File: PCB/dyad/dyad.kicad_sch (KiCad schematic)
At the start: 7 parts, among them SW1 SW_SPST, SW2 SW_SPST, SW3 SW_SPST, SW4 SW_SPST, SW5 SW_SPST, SW6 SW_SPST

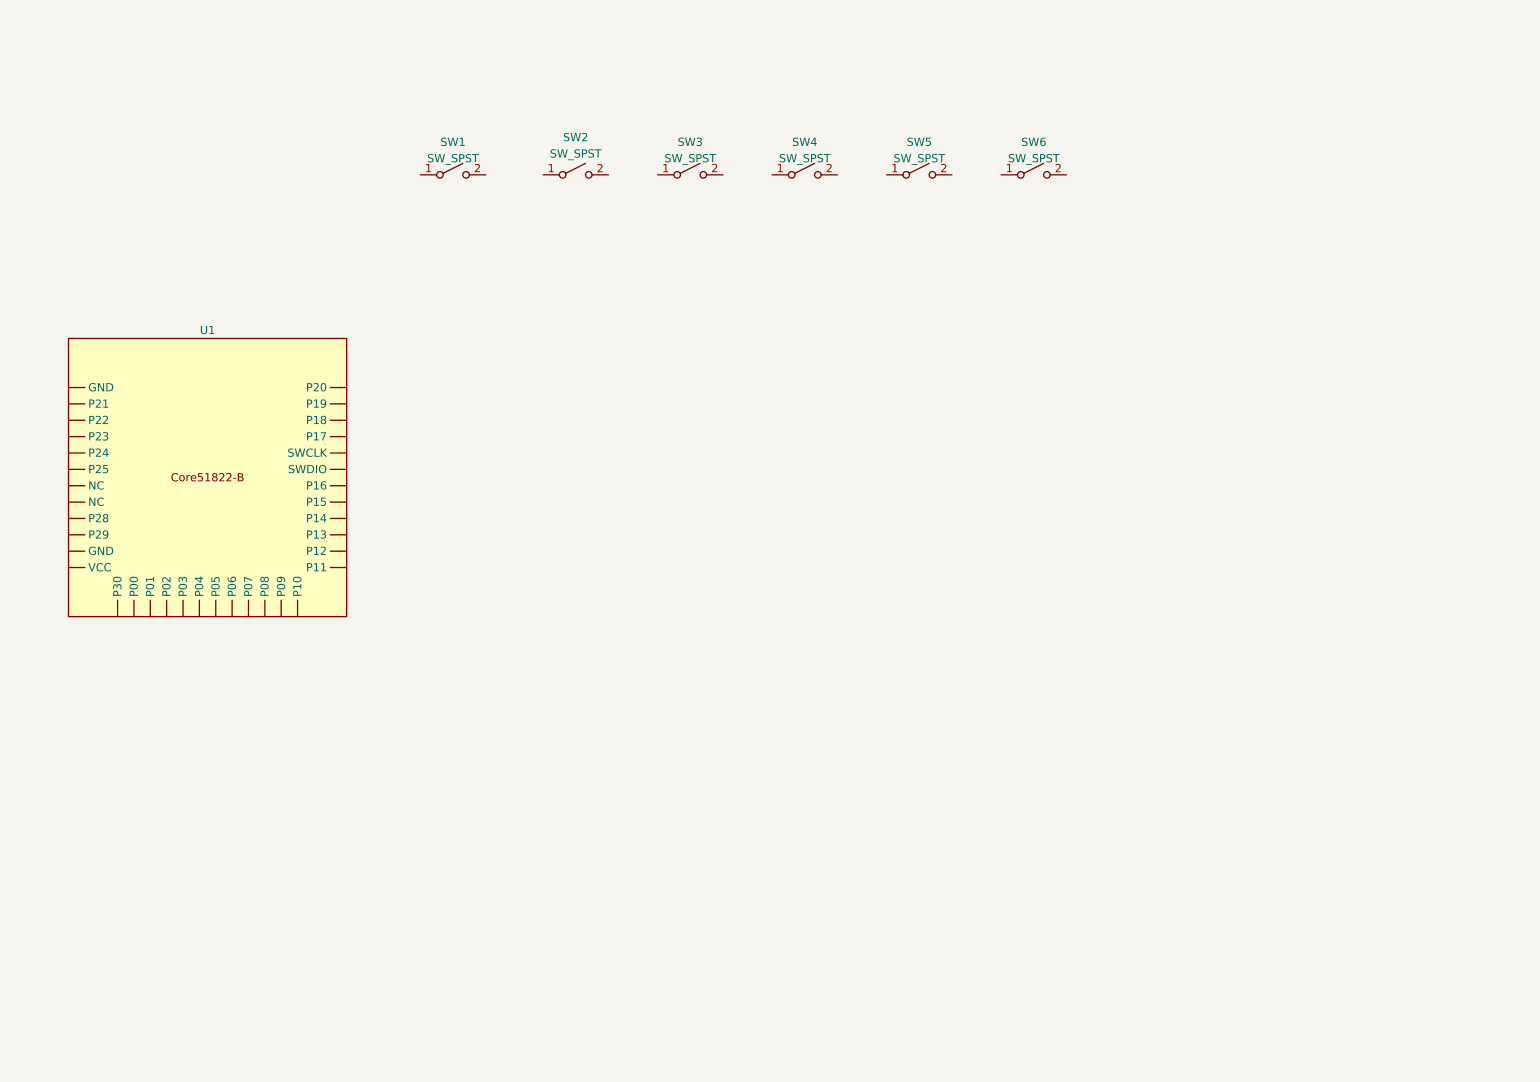
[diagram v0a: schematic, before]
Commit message: add diodes
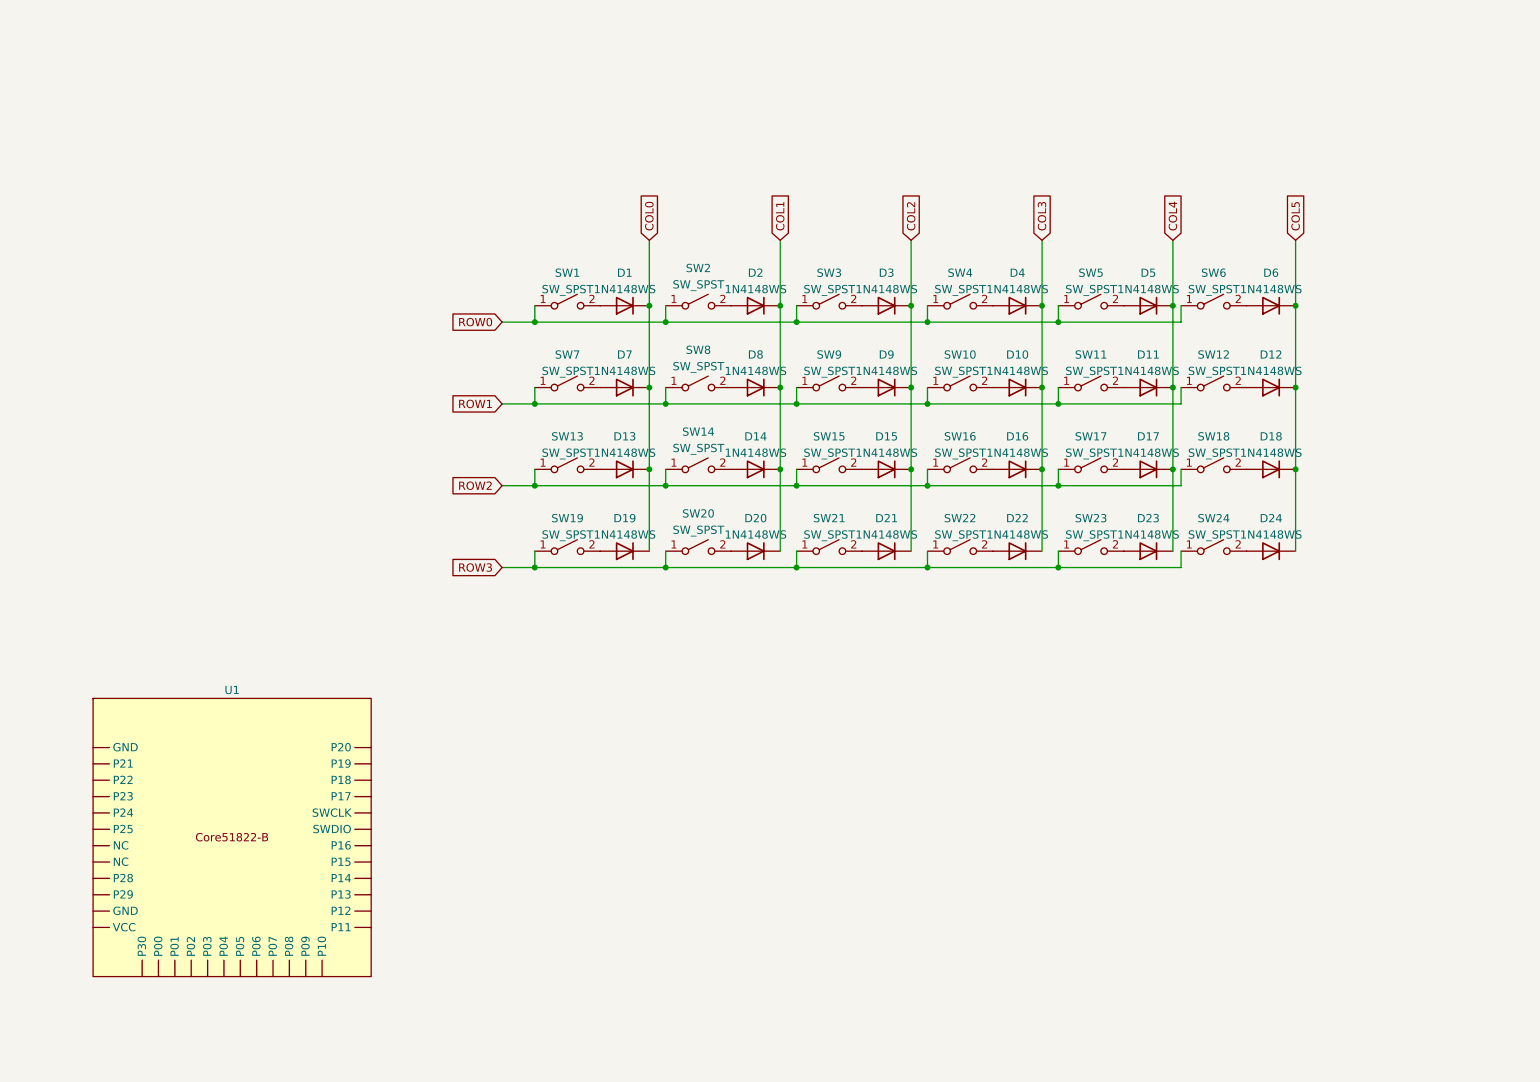
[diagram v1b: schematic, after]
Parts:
- added D1, D10, D11, D12, D13, D14, D15, D16, D17, D18, D19, D2, D20, D21, D22, D23, D24, D3, D4, D5, D6, D7, D8, D9: 1N4148WS, Diode_SMD:D_SOD-323, symbol Diode:1N4148WS
- added SW10, SW11, SW12, SW13, SW14, SW15, SW16, SW17, SW18, SW19, SW20, SW21, SW22, SW23, SW24, SW7, SW8, SW9: SW_SPST, keyswitches.pretty-master:Kailh_socket_MX, symbol Switch:SW_SPST
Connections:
- net ROW0: now reaches SW6.1 (A)
- net ROW0: now also SW1.1 (A), SW2.1 (A), SW3.1 (A), SW4.1 (A), SW5.1 (A)
- net at SW6.2 (B): now also D6.2 (A)
- net at SW5.2 (B): now also D5.2 (A)
- net at SW1.2 (B): now also D1.2 (A)
- net at SW3.2 (B): now also D3.2 (A)
- net at SW2.2 (B): now also D2.2 (A)
- net at SW4.2 (B): now also D4.2 (A)
- new net: D22.2 (A), SW22.2 (B)
- new net: D21.2 (A), SW21.2 (B)
- new net: D15.2 (A), SW15.2 (B)
- new net: D16.2 (A), SW16.2 (B)
- new net: D10.2 (A), SW10.2 (B)
- new net: D9.2 (A), SW9.2 (B)
- new net: D11.2 (A), SW11.2 (B)
- new net: D23.2 (A), SW23.2 (B)
- new net: D18.2 (A), SW18.2 (B)
- new net: D24.2 (A), SW24.2 (B)
- new net: D8.2 (A), SW8.2 (B)
- new net: D20.2 (A), SW20.2 (B)
- new net: D12.2 (A), SW12.2 (B)
- new net: D14.2 (A), SW14.2 (B)
- new net: D19.2 (A), SW19.2 (B)
- new net: D17.2 (A), SW17.2 (B)
- new net: D13.2 (A), SW13.2 (B)
- new net: D7.2 (A), SW7.2 (B)
- new net COL0: D1.1 (K), D13.1 (K), D19.1 (K), D7.1 (K)
- new net COL1: D14.1 (K), D2.1 (K), D20.1 (K), D8.1 (K)
- new net COL2: D15.1 (K), D21.1 (K), D3.1 (K), D9.1 (K)
- new net COL3: D10.1 (K), D16.1 (K), D22.1 (K), D4.1 (K)
- new net COL4: D11.1 (K), D17.1 (K), D23.1 (K), D5.1 (K)
- new net COL5: D12.1 (K), D18.1 (K), D24.1 (K), D6.1 (K)
- new net ROW1: SW10.1 (A), SW11.1 (A), SW12.1 (A), SW7.1 (A), SW8.1 (A), SW9.1 (A)
- new net ROW2: SW13.1 (A), SW14.1 (A), SW15.1 (A), SW16.1 (A), SW17.1 (A), SW18.1 (A)
- new net ROW3: SW19.1 (A), SW20.1 (A), SW21.1 (A), SW22.1 (A), SW23.1 (A), SW24.1 (A)
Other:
- moved on the sheet: SW1, SW2, SW3, SW4, SW5, SW6, U1

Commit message: added mounting holes
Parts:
- added BT1: Battery_Cell, lcsc:MY-2032-31, symbol Device:Battery_Cell
- added H1, H2, H3, H4, H5: MountingHole, MountingHole:MountingHole_2mm, symbol Mechanical:MountingHole
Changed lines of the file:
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@@
+    )
+  )
+  (symbol (lib_id "Mechanical:MountingHole") (at 176.53 119.38 0) (unit 1)
+    (in_bom yes) (on_board yes) (dnp no) (fields_autoplaced)
+    (property "Reference" "H2" (at 179.07 118.745 0)
+      (effects (font (size 1.27 1.27)) (justify left))
+    )
+    (property "Value" "MountingHole" (at 179.07 121.285 0)
+      (effects (font (size 1.27 1.27)) (justify left))
+    )
+    (property "Footprint" "MountingHole:MountingHole_2mm" (at 176.53 119.38 0)
+      (effects (font (size 1.27 1.27)) hide)
+    )
+    (property "Datasheet" "~" (at 176.53 119.38 0)
+      (effects (font (size 1.27 1.27)) hide)
+    )
+    (instances
+      (project "dyad"
+        (path "/de8492ac-3d61-4486-b710-a77ceb3d7c31"
+          (reference "H2") (unit 1)
+        )
+      )
     )
   )
@@
     )
   )
+  (symbol (lib_id "Mechanical:MountingHole") (at 158.75 129.54 0) (unit 1)
+    (in_bom yes) (on_board yes) (dnp no) (fields_autoplaced)
+    (property "Reference" "H3" (at 161.29 128.905 0)
+      (effects (font (size 1.27 1.27)) (justify left))
+    )
+    (property "Value" "MountingHole" (at 161.29 131.445 0)
+      (effects (font (size 1.27 1.27)) (justify left))
+    )
+    (property "Footprint" "MountingHole:MountingHole_2mm" (at 158.75 129.54 0)
+      (effects (font (size 1.27 1.27)) hide)
+    )
+    (property "Datasheet" "~" (at 158.75 129.54 0)
+      (effects (font (size 1.27 1.27)) hide)
+    )
+    (instances
+      (project "dyad"
+        (path "/de8492ac-3d61-4486-b710-a77ceb3d7c31"
+          (reference "H3") (unit 1)
+        )
+      )
+    )
+  )
   (symbol (lib_id "Switch:SW_SPST") (at 203.2 99.06 0) (unit 1)
     (in_bom yes) (on_board yes) (dnp no) (fields_autoplaced)
@@
     )
   )
+  (symbol (lib_id "Device:Battery_Cell") (at 121.92 138.43 0) (unit 1)
+    (in_bom yes) (on_board yes) (dnp no) (fields_autoplaced)
+    (property "Reference" "BT1" (at 125.73 135.763 0)
+      (effects (font (size 1.27 1.27)) (justify left))
+    )
+    (property "Value" "Battery_Cell" (at 125.73 138.303 0)
+      (effects (font (size 1.27 1.27)) (justify left))
+    )
+    (property "Footprint" "lcsc:MY-2032-31" (at 121.92 136.906 90)
+      (effects (font (size 1.27 1.27)) hide)
+    )
+    (property "Datasheet" "~" (at 121.92 136.906 90)
+      (effects (font (size 1.27 1.27)) hide)
+    )
+    (pin "1")
+    (pin "2")
+    (instances
+      (project "dyad"
+        (path "/de8492ac-3d61-4486-b710-a77ceb3d7c31"
+          (reference "BT1") (unit 1)
+        )
+      )
+    )
+  )
   (symbol (lib_id "Diode:1N4148WS") (at 172.72 86.36 180) (unit 1)
     (in_bom yes) (on_board yes) (dnp no) (fields_autoplaced)
@@
     )
   )
+  (symbol (lib_id "Mechanical:MountingHole") (at 176.53 129.54 0) (unit 1)
+    (in_bom yes) (on_board yes) (dnp no) (fields_autoplaced)
+    (property "Reference" "H4" (at 179.07 128.905 0)
+      (effects (font (size 1.27 1.27)) (justify left))
+    )
+    (property "Value" "MountingHole" (at 179.07 131.445 0)
+      (effects (font (size 1.27 1.27)) (justify left))
+    )
+    (property "Footprint" "MountingHole:MountingHole_2mm" (at 176.53 129.54 0)
+      (effects (font (size 1.27 1.27)) hide)
+    )
+    (property "Datasheet" "~" (at 176.53 129.54 0)
+      (effects (font (size 1.27 1.27)) hide)
+    )
+    (instances
+      (project "dyad"
+        (path "/de8492ac-3d61-4486-b710-a77ceb3d7c31"
+          (reference "H4") (unit 1)
+        )
+      )
+    )
+  )
+  (symbol (lib_id "Mechanical:MountingHole") (at 158.75 119.38 0) (unit 1)
+    (in_bom yes) (on_board yes) (dnp no) (fields_autoplaced)
+    (property "Reference" "H1" (at 161.29 118.745 0)
+      (effects (font (size 1.27 1.27)) (justify left))
+    )
+    (property "Value" "MountingHole" (at 161.29 121.285 0)
+      (effects (font (size 1.27 1.27)) (justify left))
+    )
+    (property "Footprint" "MountingHole:MountingHole_2mm" (at 158.75 119.38 0)
+      (effects (font (size 1.27 1.27)) hide)
+    )
+    (property "Datasheet" "~" (at 158.75 119.38 0)
+      (effects (font (size 1.27 1.27)) hide)
+    )
+    (instances
+      (project "dyad"
+        (path "/de8492ac-3d61-4486-b710-a77ceb3d7c31"
+          (reference "H1") (unit 1)
+        )
+      )
+    )
+  )
   (symbol (lib_id "Switch:SW_SPST") (at 184.15 99.06 0) (unit 1)
     (in_bom yes) (on_board yes) (dnp no) (fields_autoplaced)
@@
         )
       )
+    )
+  )
+  (symbol (lib_id "Mechanical:MountingHole") (at 167.64 124.46 0) (unit 1)
+    (in_bom yes) (on_board yes) (dnp no) (fields_autoplaced)
+    (property "Reference" "H5" (at 170.18 123.825 0)
+      (effects (font (size 1.27 1.27)) (justify left))
+    )
+    (property "Value" "MountingHole" (at 170.18 126.365 0)
+      (effects (font (size 1.27 1.27)) (justify left))
+    )
+    (property "Footprint" "MountingHole:MountingHole_2mm" (at 167.64 124.46 0)
+      (effects (font (size 1.27 1.27)) hide)
+    )
+    (property "Datasheet" "~" (at 167.64 124.46 0)
+      (effects (font (size 1.27 1.27)) hide)
+    )
+    (instances
+      (project "dyad"
+        (path "/de8492ac-3d61-4486-b710-a77ceb3d7c31"
+          (reference "H5") (unit 1)
+        )
+      )

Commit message: Update dyad.kicad_sch
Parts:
- removed BT1: Battery_Cell, lcsc:MY-2032-31, symbol Device:Battery_Cell
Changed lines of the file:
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@@
-    )
-  )
-  (symbol (lib_id "Device:Battery_Cell") (at 121.92 138.43 0) (unit 1)
-    (in_bom yes) (on_board yes) (dnp no) (fields_autoplaced)
-    (property "Reference" "BT1" (at 125.73 135.763 0)
-      (effects (font (size 1.27 1.27)) (justify left))
-    )
-    (property "Value" "Battery_Cell" (at 125.73 138.303 0)
-      (effects (font (size 1.27 1.27)) (justify left))
-    )
-    (property "Footprint" "lcsc:MY-2032-31" (at 121.92 136.906 90)
-      (effects (font (size 1.27 1.27)) hide)
-    )
-    (property "Datasheet" "~" (at 121.92 136.906 90)
-      (effects (font (size 1.27 1.27)) hide)
-    )
-    (pin "1")
-    (pin "2")
-    (instances
-      (project "dyad"
-        (path "/de8492ac-3d61-4486-b710-a77ceb3d7c31"
-          (reference "BT1") (unit 1)
-        )
-      )
     )
   )

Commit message: update pcb and schematic
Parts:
- added BT1: Battery_Cell, lcsc:MY-2032-31, symbol Device:Battery_Cell
- added CHG1, PRG1: Conn_01x04_Pin, Connector_PinHeader_2.54mm:PinHeader_1x04_P2.54mm_Vertical, symbol Connector:Conn_01x04_Pin
- renumbered D24 to D1, D15 to D10, D14 to D11, D13 to D12, D12 to D13, D11 to D14, D10 to D15, D9 to D16, D8 to D17, D7 to D18, D6 to D19, D23 to D2, D5 to D20, D4 to D21, D3 to D22, D2 to D23, D1 to D24, D22 to D3, D21 to D4, D20 to D5, D19 to D6, D18 to D7, D17 to D8, D16 to D9, SW24 to SW1, SW15 to SW10, SW14 to SW11, SW13 to SW12, SW12 to SW13, SW11 to SW14, SW10 to SW15, SW9 to SW16, SW8 to SW17, SW7 to SW18, SW6 to SW19, SW23 to SW2, SW5 to SW20, SW4 to SW21, SW3 to SW22, SW2 to SW23, SW1 to SW24, SW22 to SW3, SW21 to SW4, SW20 to SW5, SW19 to SW6, SW18 to SW7, SW17 to SW8, SW16 to SW9
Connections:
- net COL0: now also D1.1 (K), D13.1 (K), D19.1 (K), D7.1 (K), U1.29 (P16); no longer D12.1 (K), D18.1 (K), D24.1 (K), D6.1 (K)
- net COL1: now also D14.1 (K), D2.1 (K), D20.1 (K), D8.1 (K), U1.28 (P15); no longer D11.1 (K), D17.1 (K), D23.1 (K), D5.1 (K)
- net COL2: now also D15.1 (K), D21.1 (K), D3.1 (K), D9.1 (K), U1.27 (P14); no longer D10.1 (K), D16.1 (K), D22.1 (K), D4.1 (K)
- net COL3: now also D10.1 (K), D16.1 (K), D22.1 (K), D4.1 (K), U1.26 (P13); no longer D15.1 (K), D21.1 (K), D3.1 (K), D9.1 (K)
- net COL4: now also D11.1 (K), D17.1 (K), D23.1 (K), D5.1 (K), U1.25 (P12); no longer D14.1 (K), D2.1 (K), D20.1 (K), D8.1 (K)
- net COL5: now also D12.1 (K), D18.1 (K), D24.1 (K), D6.1 (K), U1.24 (P11); no longer D1.1 (K), D13.1 (K), D19.1 (K), D7.1 (K)
- net ROW0: now also SW1.1 (A), SW2.1 (A), SW3.1 (A), SW4.1 (A), SW5.1 (A), SW6.1 (A), U1.15 (P02); no longer SW19.1 (A), SW20.1 (A), SW21.1 (A), SW22.1 (A), SW23.1 (A), SW24.1 (A)
- net ROW1: now also SW10.1 (A), SW11.1 (A), SW12.1 (A), SW7.1 (A), SW8.1 (A), SW9.1 (A), U1.14 (P01); no longer SW13.1 (A), SW14.1 (A), SW15.1 (A), SW16.1 (A), SW17.1 (A), SW18.1 (A)
- net ROW2: now also SW13.1 (A), SW14.1 (A), SW15.1 (A), SW16.1 (A), SW17.1 (A), SW18.1 (A), U1.13 (P00); no longer SW10.1 (A), SW11.1 (A), SW12.1 (A), SW7.1 (A), SW8.1 (A), SW9.1 (A)
- net ROW3: now also SW19.1 (A), SW20.1 (A), SW21.1 (A), SW22.1 (A), SW23.1 (A), SW24.1 (A), U1.12 (P30); no longer SW1.1 (A), SW2.1 (A), SW3.1 (A), SW4.1 (A), SW5.1 (A), SW6.1 (A)
- new net B+: BT1.1 (+), CHG1.2 (Pin_2)
- new net B-: BT1.2 (-), CHG1.3 (Pin_3)
- new net GND: CHG1.4 (Pin_4), PRG1.1 (Pin_1), U1.0 (GND), U1.10 (GND)
- new net SWCLK: PRG1.2 (Pin_2), U1.31 (SWCLK)
- new net SWDIO: PRG1.3 (Pin_3), U1.30 (SWDIO)
- new net VCC: CHG1.1 (Pin_1), PRG1.4 (Pin_4), U1.11 (VCC)
- no-connect marks 0 -> 2
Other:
- moved on the sheet: D1, D10, D11, D12, D13, D14, D15, D16, D17, D18, D19, D2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
